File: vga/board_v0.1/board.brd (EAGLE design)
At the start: 35 x 42 mm, 13 parts

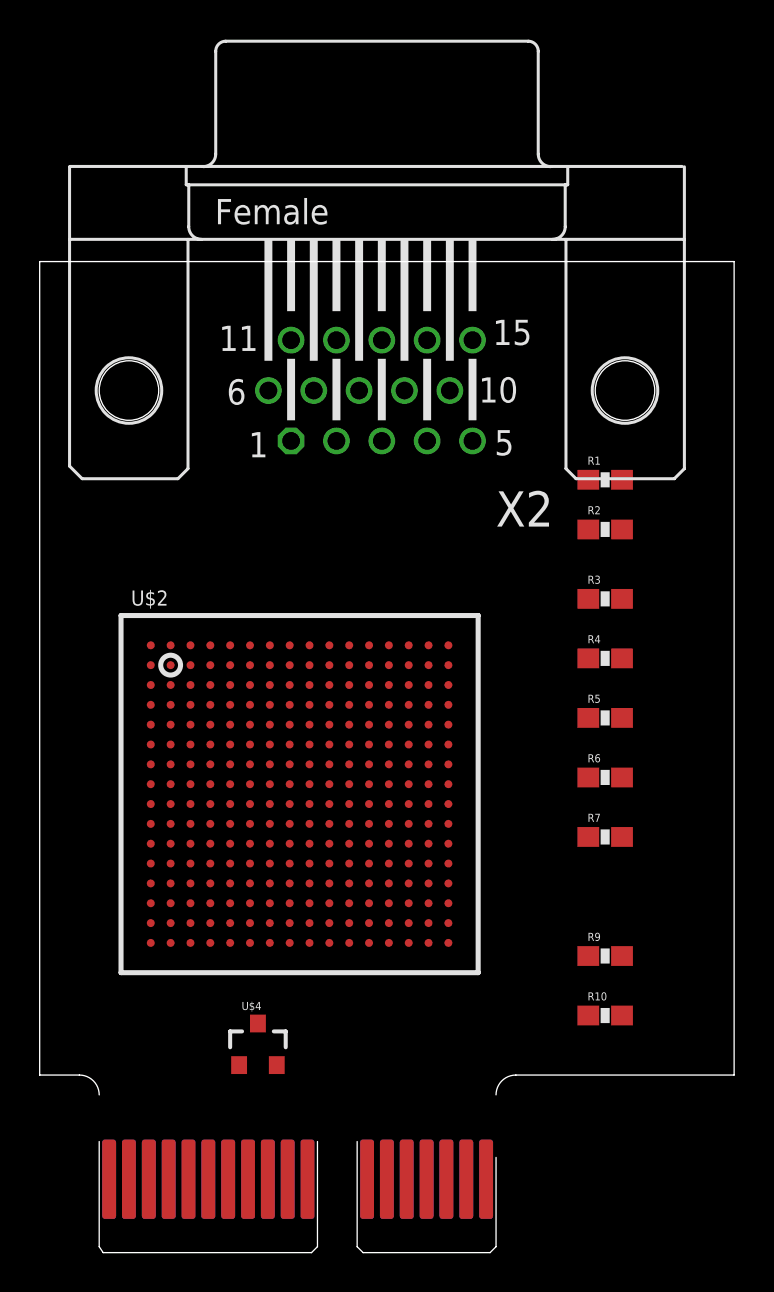
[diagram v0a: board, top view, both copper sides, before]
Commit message: vga card done -- first 4-layer board!
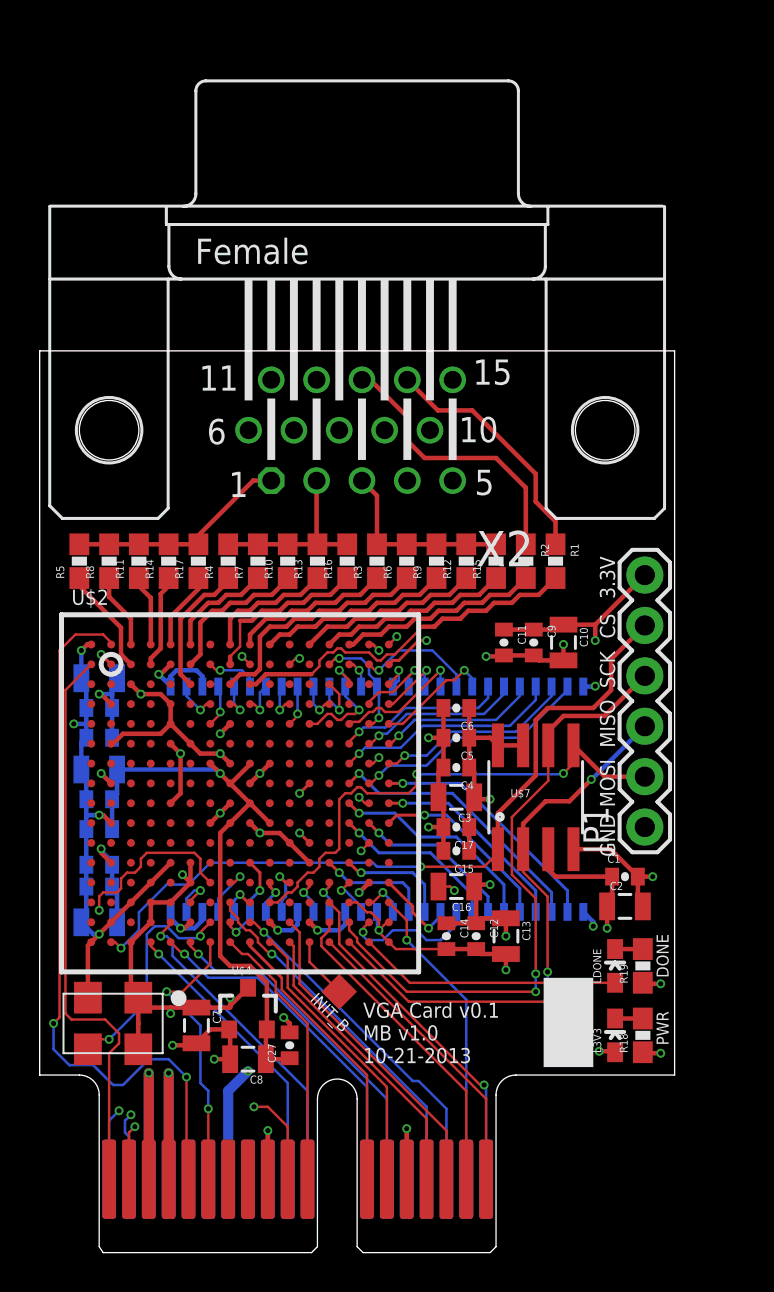
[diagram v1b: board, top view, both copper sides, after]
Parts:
- added C1, C11, C12, C14, C15, C17, C18, C20, C21, C23, C24, C26, C27, C4, C5, C6, C9: 100nF, kmod-passives:0402-CAP
- added C10, C13, C16, C19, C2, C22, C25, C3, C7, C8: 10uF, kmod-passives:0805
- added IC1: AS4C4M16S, memory-micron:TSOP54-400
- added INIT_B: (no value), kmod-nonparts:TESTPAD-1.27
- added JP1: (no value), SparkFun-Connectors:1X06
- added L3V3, LDONE: YLW, kmod-passives:0603_LED
- added R11: 2k, kmod-passives:0603-RES
- added R12, R13, R14: 3.9k, kmod-passives:0603-RES
- added R15, R16, R17: 8.2k, kmod-passives:0603-RES
- added R18, R19: 220, kmod-passives:0603-RES
- added R8: 1k, kmod-passives:0603-RES
- added U$6: OSCILLATORCTS-636-50MHz, kmod-mechanical:CTS-636
- added U$7: S25FL, kmod-ics:SO08
- R10, R9: value 500 -> 2k
- R3: value 10 -> 510
- R4: value 500 -> 510
- R5: value 250 -> 510
- R6: value 500 -> 1k
- R7: value 250 -> 1k
- moved R10 27.9 mm to (12.5, 34.9), turned to 90 degrees
- moved R5 27.7 mm to (2.00, 34.9), turned to 90 degrees
- moved R7 22.3 mm to (11.0, 34.9), turned to 90 degrees
- moved R9 21.6 mm to (20.0, 34.9), turned to 90 degrees
- moved R4 19.6 mm to (9.50, 34.9), turned to 90 degrees
- moved R6 14.8 mm to (18.5, 34.9), turned to 90 degrees
- moved R3 11.7 mm to (17.0, 34.9), turned to 90 degrees
- moved R1 4.80 mm to (26.0, 34.9), turned to 270 degrees
- moved R2 4.31 mm to (24.5, 34.9), turned to 270 degrees
- moved U$2 3.00 mm to (10.1, 23.2)
- moved X2 2.24 mm to (16.0, 41.5)
- moved U$4 1.87 mm to (10.5, 12.3)
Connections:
- new net 50MHZ: U$2.R7, U$6.3
- new net A0: U$1.A15, U$2.P8
- new net A1: U$1.A16, U$2.R9
- new net A2: U$1.A17, U$2.P16
- new net A3: U$1.A18, U$2.P13
- new net B0: U$1.B15, U$2.T11
- new net B1: U$1.B16, U$2.R11
- new net B2: U$1.B17, U$2.R13
- new net B3: U$1.B18, U$2.T13
- new net C0: U$1.A10, U$2.T4
- new net C1: U$1.A11, U$2.R5
- new net C2: U$1.A12, U$2.T5
- new net C3: U$1.A13, U$2.T6
- new net CS: JP1.5, U$2.T2, U$7.1
- new net D0: U$1.B10, U$2.N7
- new net D1: U$1.B11, U$2.T8
- new net D2: U$1.B12, U$2.T9
- new net D3: U$1.B13, U$2.T10
- new net DONE: LDONE.A, U$2.T15
- new net G0: U$1.B6, U$2.T7
- new net GRST: U$1.B5, U$2.A2
- new net MA0: IC1.23, U$2.F16
- new net MA1: IC1.24, U$2.G14
- new net MA10: IC1.22, U$2.F15
- new net MA11: IC1.35, U$2.K14
- new net MA12: IC1.36, U$2.R15
- new net MA2: IC1.25, U$2.G16
- new net MA3: IC1.26, U$2.H15
- new net MA4: IC1.29, U$2.H16
- new net MA5: IC1.30, U$2.H14
- new net MA6: IC1.31, U$2.J16
- new net MA7: IC1.32, U$2.K16
- new net MA8: IC1.33, U$2.J14
- new net MA9: IC1.34, U$2.K15
- new net MBA0: IC1.20, U$2.E16
- new net MBA1: IC1.21, U$2.F14
- new net MCAS: IC1.17, U$2.D16
- new net MCKE: IC1.37, U$2.N16
- new net MCLK: IC1.38, U$2.M14
- new net MCS: IC1.19, U$2.B15
- new net MDQ0: IC1.2, U$2.D7
- new net MDQ1: IC1.4, U$2.E7
- new net MDQ10: IC1.45, U$2.N12
- new net MDQ11: IC1.47, U$2.N11
- new net MDQ12: IC1.48, U$2.N10
- new net MDQ13: IC1.50, U$2.P9
- new net MDQ14: IC1.51, U$2.N8
- new net MDQ15: IC1.53, U$2.P6
- new net MDQ2: IC1.5, U$2.D8
- new net MDQ3: IC1.7, U$2.D9
- new net MDQ4: IC1.8, U$2.D11
- new net MDQ5: IC1.10, U$2.D13
- new net MDQ6: IC1.11, U$2.C13
- new net MDQ7: IC1.13, U$2.B14
- new net MDQ8: IC1.42, U$2.N14
- new net MDQ9: IC1.44, U$2.N13
- new net MDQMH: IC1.39, U$2.M13
- new net MDQML: IC1.15, U$2.C16
- new net MISO: JP1.3, U$2.T14, U$7.2
- new net MNC: IC1.40, U$2.P15
- new net MOSI: JP1.2, U$2.P10, U$7.5
- new net MRAS: IC1.18, U$2.E14
- new net MWE: IC1.16, U$2.D15
- new net N$6: L3V3.C, R18.2
- new net N$7: R10.2, R13.2, R16.2, R4.2, R7.2, X2.2
- new net N$8: R11.2, R14.2, R17.2, R5.2, R8.2, X2.1
- new net SCK: JP1.4, U$2.R14, U$7.6
- new net VB0: R3.1, U$2.A9
- new net VB1: R6.1, U$2.C8
- new net VB2: R9.1, U$2.A10
- new net VB3: R12.1, U$2.A12
- new net VB4: R15.1, U$2.A13
- new net VG0: R4.1, U$2.C6
- new net VG1: R7.1, U$2.A6
- new net VG2: R10.1, U$2.B6
- new net VG3: R13.1, U$2.A8
- new net VG4: R16.1, U$2.B8
- new net VR0: R5.1, U$2.B3
- new net VR1: R8.1, U$2.A3
- new net VR2: R11.1, U$2.A4
- new net VR3: R14.1, U$2.B4
- new net VR4: R17.1, U$2.A5
- net 1.2V: now also C24.1, C25.1, C26.1, C27.1, C8.1
- net 3.3V: now also C1.1, C10.1, C11.1, C12.1, C13.1, C14.1, C15.1, C16.1, C17.1, C18.1, C19.1, C2.1, C20.1, C21.1, C22.1, C23.1, C3.1, C4.1, C5.1, C6.1, C7.1, C9.1, IC1.1, IC1.14, IC1.27, IC1.3, IC1.43, IC1.49, IC1.9, JP1.6, L3V3.A, U$2.N6, U$2.P4, U$2.P5, U$2.T3, U$6.1, U$6.4, U$7.3, U$7.7, U$7.8
- net GND: now also C1.2, C10.2, C11.2, C12.2, C13.2, C14.2, C15.2, C16.2, C17.2, C18.2, C19.2, C2.2, C20.2, C21.2, C22.2, C23.2, C24.2, C25.2, C26.2, C27.2, C3.2, C4.2, C5.2, C6.2, C7.2, C8.2, C9.2, IC1.12, IC1.28, IC1.41, IC1.46, IC1.52, IC1.54, IC1.6, JP1.1, R18.1, R19.1, U$1.A14, U$1.A9, U$1.B14, U$1.B9, U$2.D5, U$2.N4, U$2.R16, U$2.R2, U$6.2, U$7.4
- net HSYNC: now also U$2.A14
- net N$3: now also LDONE.C, R19.2; no longer X2.1
- net N$4: now also INIT_B.P, U$2.T12; no longer X2.2
- net N$5: now also R12.2, R15.2, R3.2, R6.2, R9.2
- net VSYNC: now also U$2.C9
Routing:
- net GND: track 0.00 -> 139.6 mm, vias 0 -> 36
- net 3.3V: track 0.00 -> 97.7 mm, vias 0 -> 28
- net TDO: track 0.00 -> 50.3 mm, vias 0 -> 2
- net TCK: track 0.00 -> 44.3 mm, vias 0 -> 2
- net CS: track 0.00 -> 38.2 mm, vias 0 -> 2
- net GRST: track 0.00 -> 37.0 mm, vias 0 -> 2
- net SCK: track 0.00 -> 31.6 mm, vias 0 -> 2
- net 1.2V: track 0.00 -> 30.4 mm, vias 0 -> 1
- net TMS: track 0.00 -> 29.8 mm, vias 0 -> 2
- net TDI: track 0.00 -> 29.0 mm
- net MISO: track 0.00 -> 28.9 mm, vias 0 -> 3
- net D0: track 0.00 -> 27.3 mm, vias 0 -> 2
- net MOSI: track 0.00 -> 25.8 mm, vias 0 -> 2
- net VSYNC: track 0.00 -> 18.3 mm
- net A0: track 0.00 -> 18.3 mm, vias 0 -> 1
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- added copper zone on layer 15, net 3.3V
- added copper zone on layer 2, net GND
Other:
- board size 35 x 42 mm -> 32 x 37.5 mm
- board text added: "3.3V"
- board text added: "CS"
- board text added: "DONE"
- board text added: "GND"
- board text added: "MISO"
- board text added: "MOSI"
- board text added: "PWR"
- board text added: "SCK"
- board text added: "VGA Card v0.1 MB v1.0 10-21-2013"
